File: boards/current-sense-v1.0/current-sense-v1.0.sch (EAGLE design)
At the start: 89 parts, among them IC1 ISO7241, IC2 ISO7241, IC3 ISO7242, IC4 ISO7240, J1 4-PIN_2MM-H, J2 MKS-1658, J3 8-PIN_2MM-H, J6 DF22-2, Q1 IRFH7545, Q2 IRFH7545, Q3 IRFH7545, Q4 IRFH7545, Q5 IRFH7545, Q6 IRFH7545, U1 DRV8303DCA, U13 TLV70233DBVR, U2 INA240PWR, U3 INA240PWR, U4 INA240PWR, U6 ADS8028IRTJT, U7 MPM3620GQV-P, U8 VND5E006ASPTR-E, U9 TLV70450

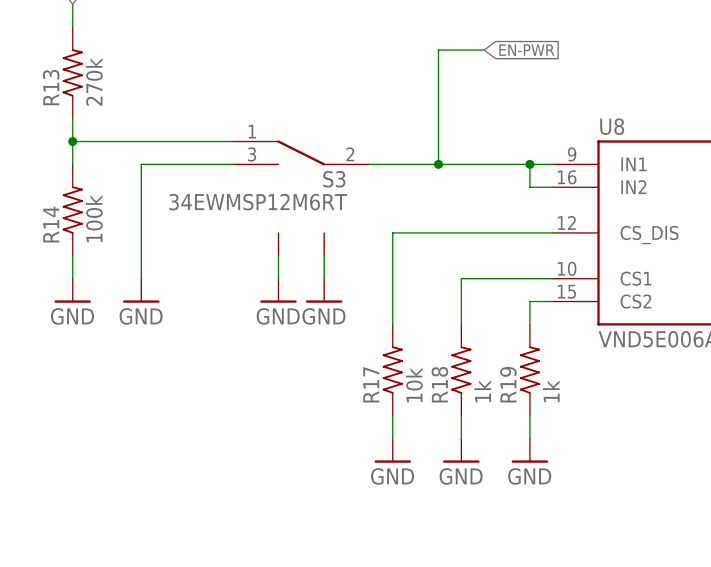
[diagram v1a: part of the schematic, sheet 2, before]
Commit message: removed two ground symbols from board
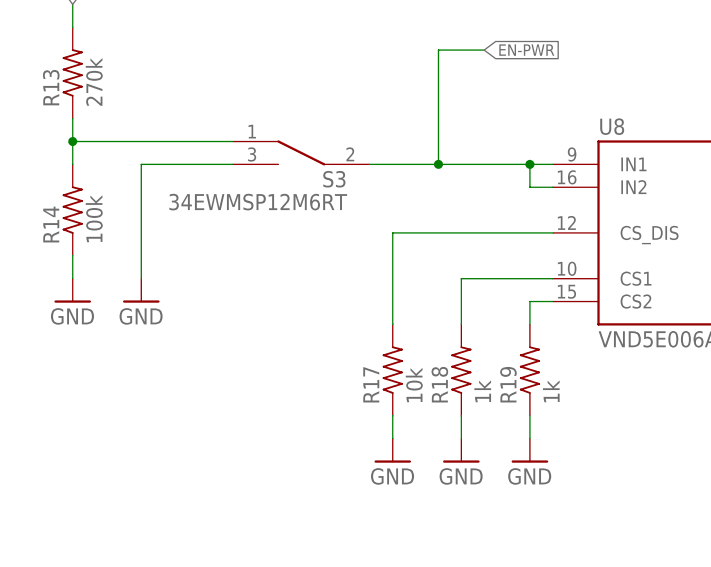
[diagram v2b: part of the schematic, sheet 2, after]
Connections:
- net GND: no longer S3G$2.LEG1, S3G$2.LEG2
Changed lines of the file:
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@@
 <part name="GND65" library="supply1" deviceset="GND" device=""/>
 <part name="S3" library="RoboJackets-Switches" deviceset="34EWMSP12M6RT" device=""/>
-<part name="GND68" library="supply1" deviceset="GND" device=""/>
-<part name="GND69" library="supply1" deviceset="GND" device=""/>
 <part name="GND66" library="supply1" deviceset="GND" device=""/>
 <part name="R22" library="rcl" deviceset="R-US_" device="R0603" value="1k"/>
@@
 <attribute name="VALUE" x="53.34" y="170.18" size="1.778" layer="96" font="vector" rot="MR0"/>
 </instance>
-<instance part="S3" gate="G$2" x="48.26" y="167.64" smashed="yes"/>
-<instance part="GND68" gate="1" x="45.72" y="160.02" smashed="yes">
-<attribute name="VALUE" x="43.18" y="157.48" size="1.778" layer="96"/>
-</instance>
-<instance part="GND69" gate="1" x="50.8" y="160.02" smashed="yes">
-<attribute name="VALUE" x="48.26" y="157.48" size="1.778" layer="96"/>
-</instance>
 <instance part="GND66" gate="1" x="30.48" y="160.02" smashed="yes">
 <attribute name="VALUE" x="27.94" y="157.48" size="1.778" layer="96"/>
@@
 </segment>
 <segment>
-<pinref part="S3" gate="G$2" pin="LEG1"/>
-<pinref part="GND68" gate="1" pin="GND"/>
-<wire x1="45.72" y1="165.1" x2="45.72" y2="162.56" width="0.1524" layer="91"/>
-</segment>
-<segment>
-<pinref part="S3" gate="G$2" pin="LEG2"/>
-<pinref part="GND69" gate="1" pin="GND"/>
-<wire x1="50.8" y1="165.1" x2="50.8" y2="162.56" width="0.1524" layer="91"/>
-</segment>
-<segment>

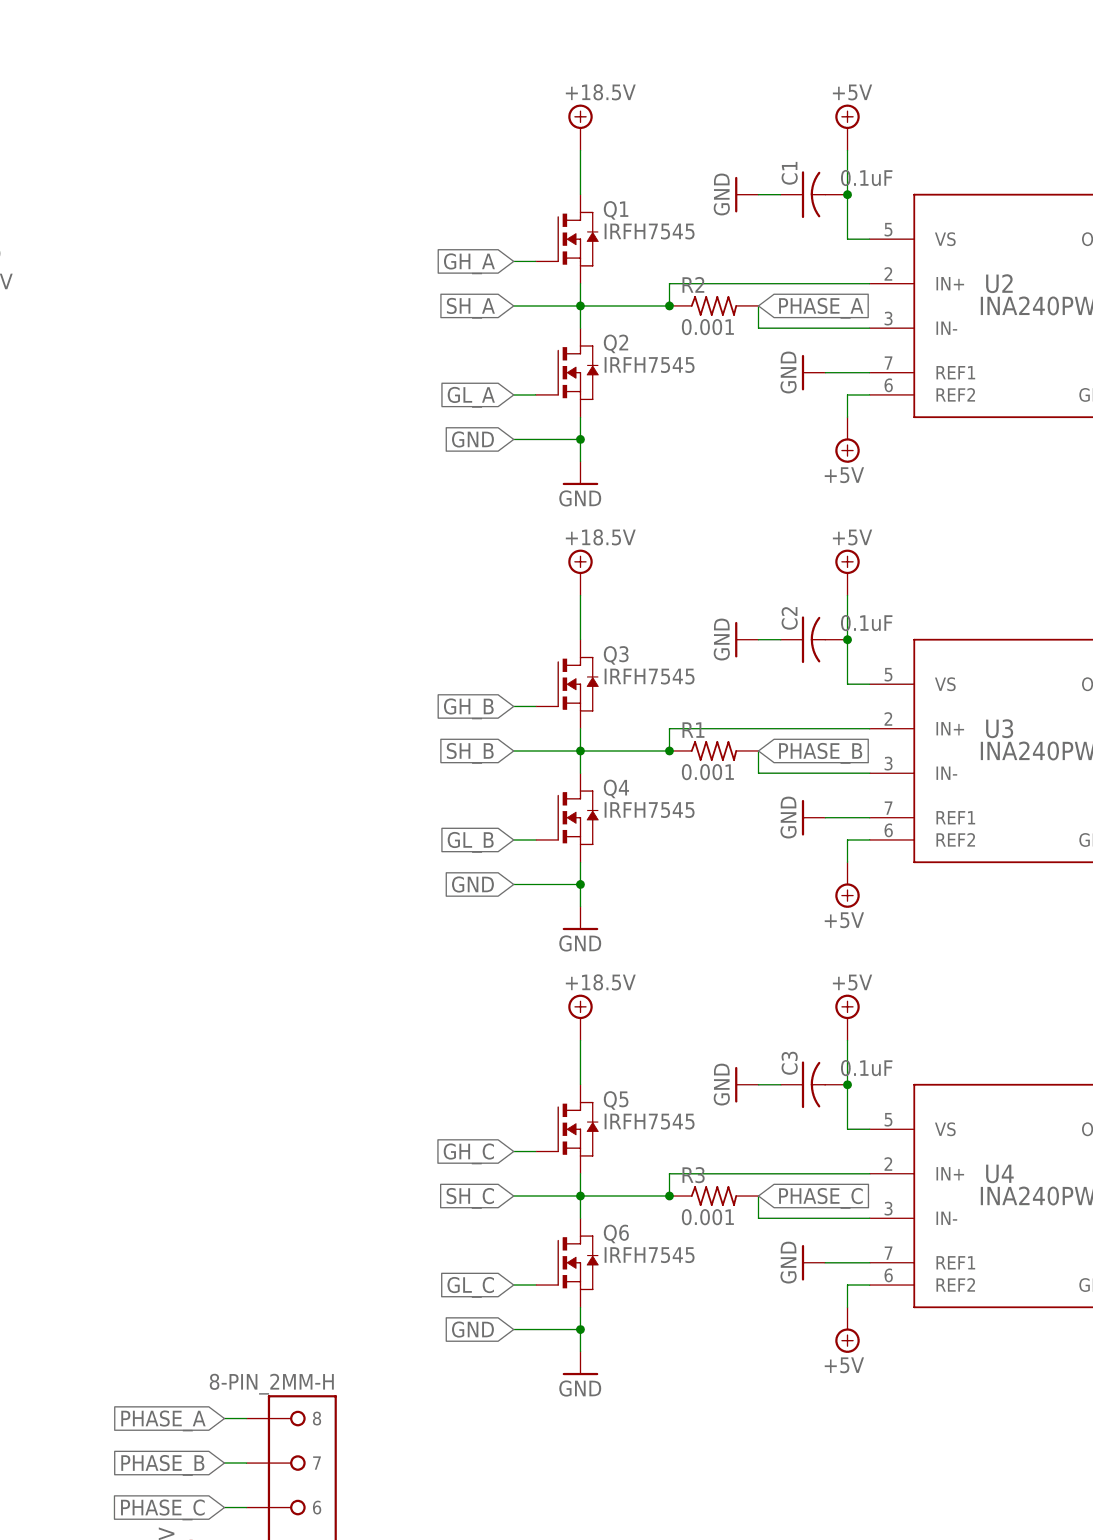
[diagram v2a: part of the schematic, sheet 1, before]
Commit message: changed supply voltage of opamps to 3V3
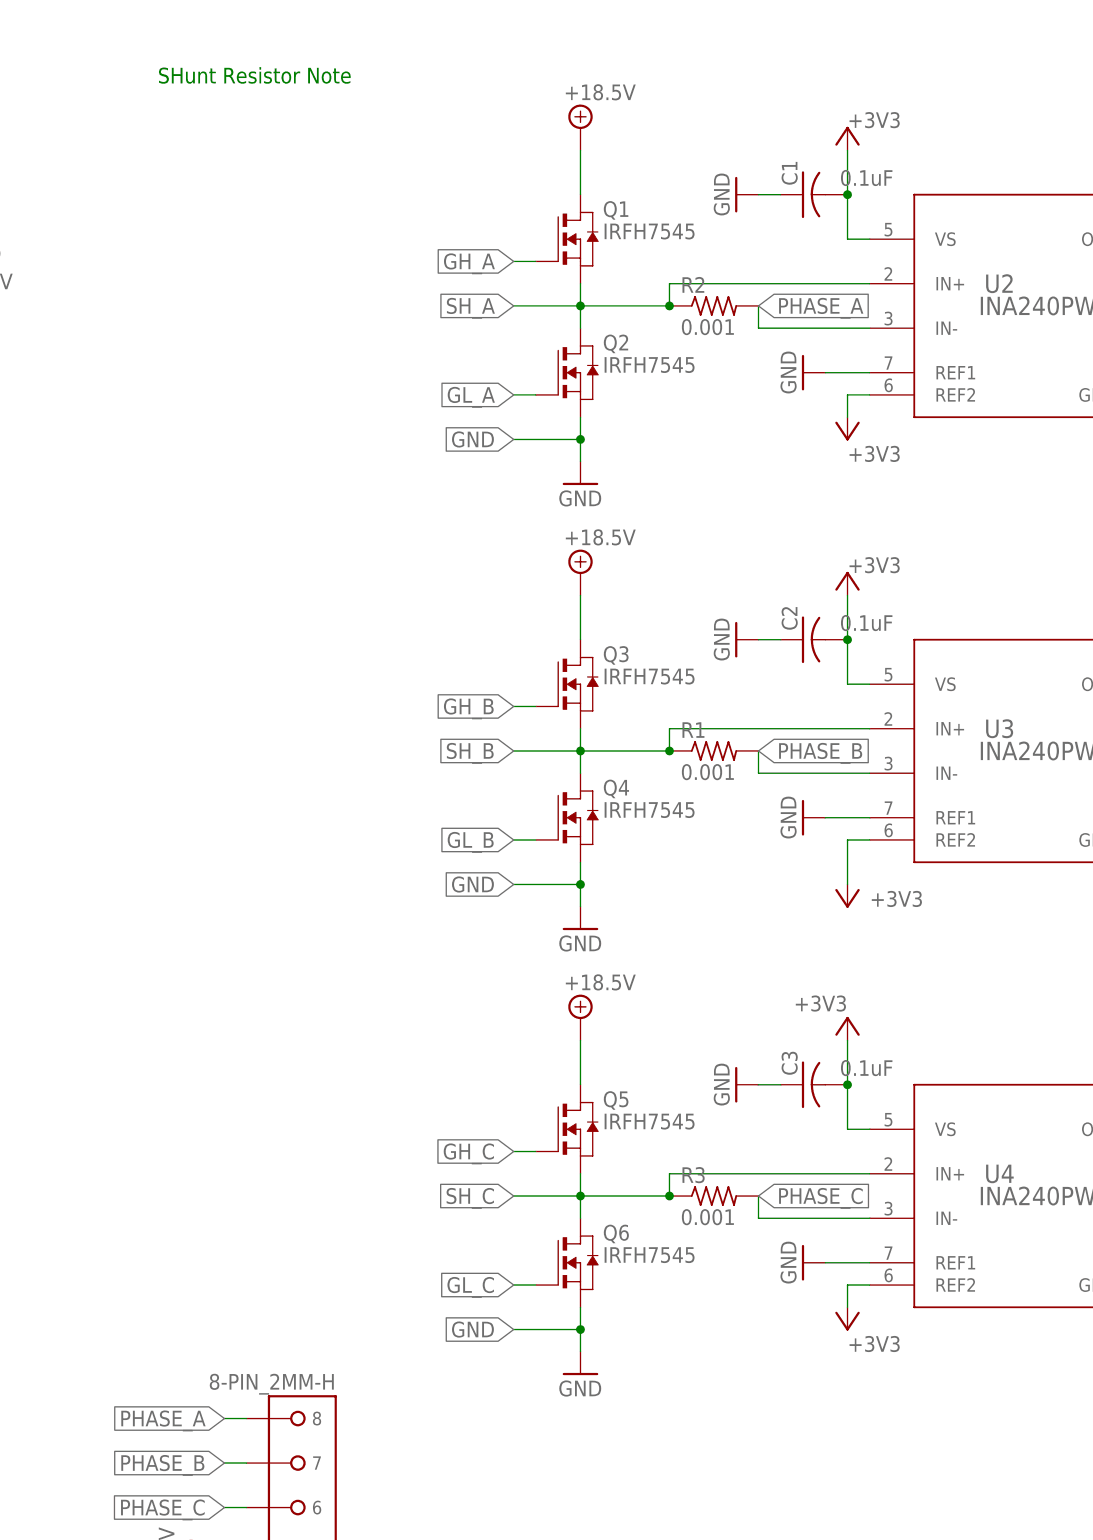
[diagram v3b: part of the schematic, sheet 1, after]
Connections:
- net ADC_5V renamed ADC_3V3
- net +3V3: now also C1.2, C2.2, C3.2, U2.REF2, U2.VS, U3.REF2, U3.VS, U4.REF2, U4.VS
- net +5V: no longer C1.2, C2.2, C3.2, U2.REF2, U2.VS, U3.REF2, U3.VS, U4.REF2, U4.VS
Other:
- note added: "SHunt Resistor Note"

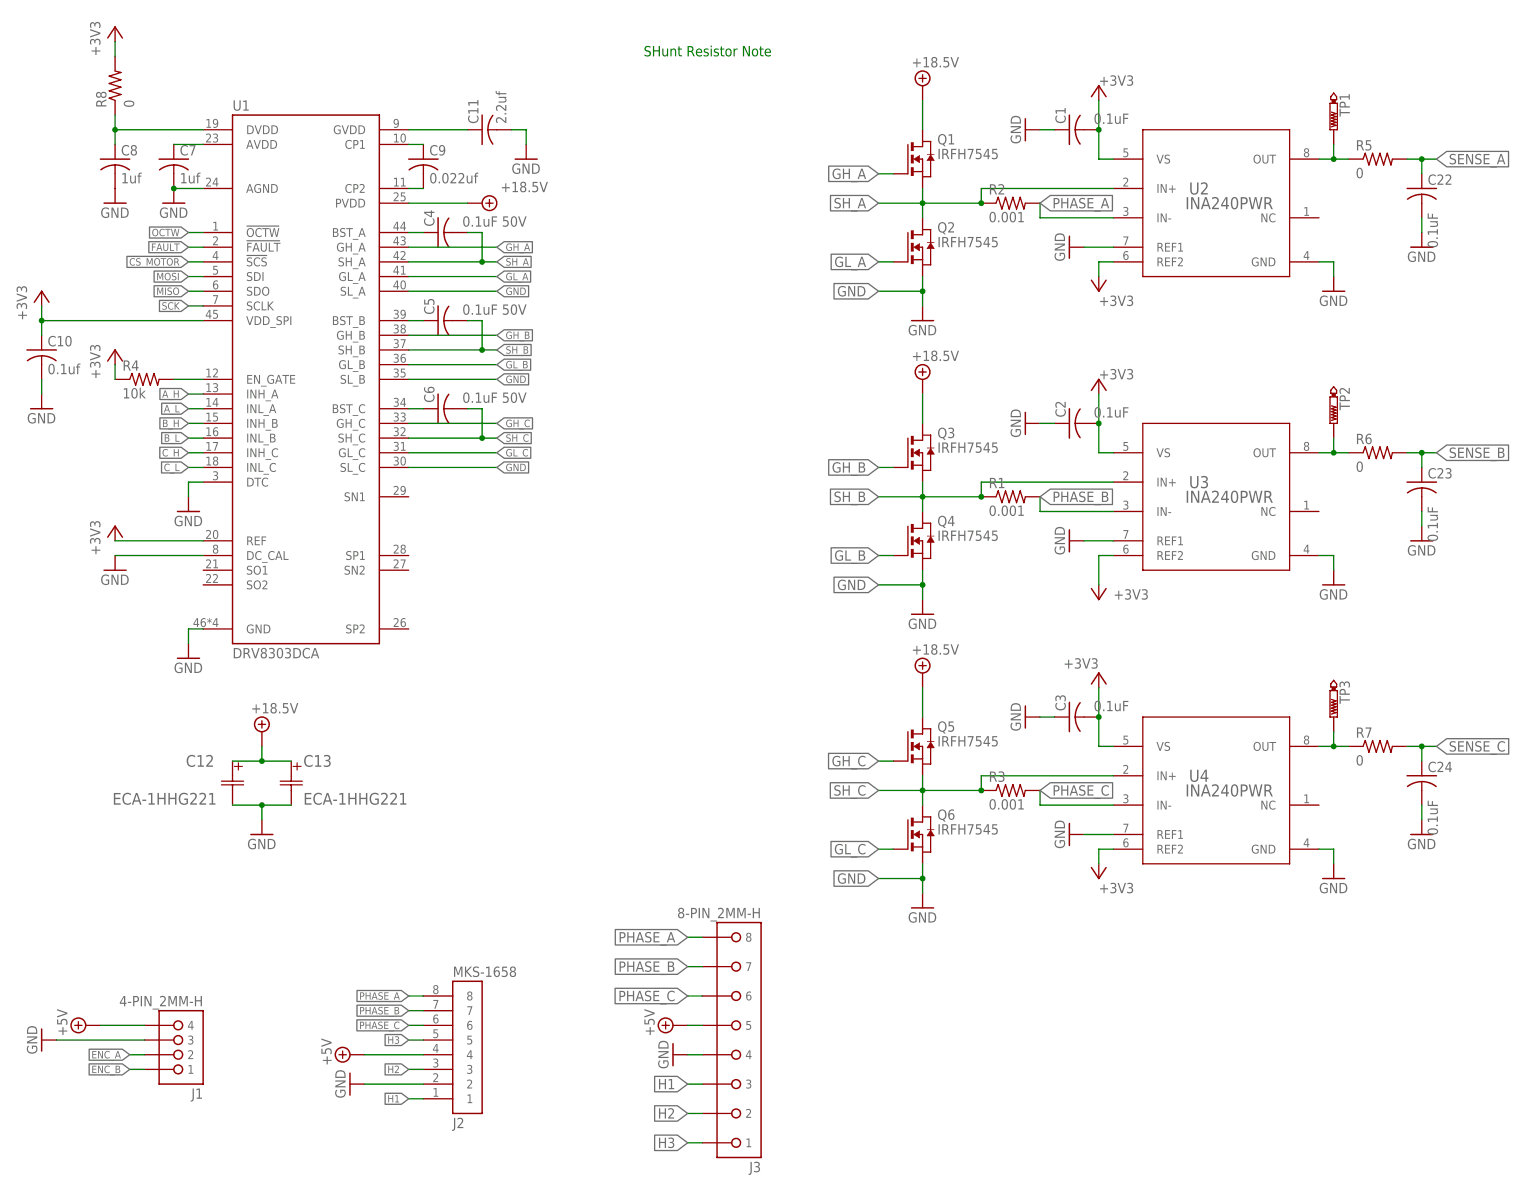
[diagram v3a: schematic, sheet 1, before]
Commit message: added borders in board view
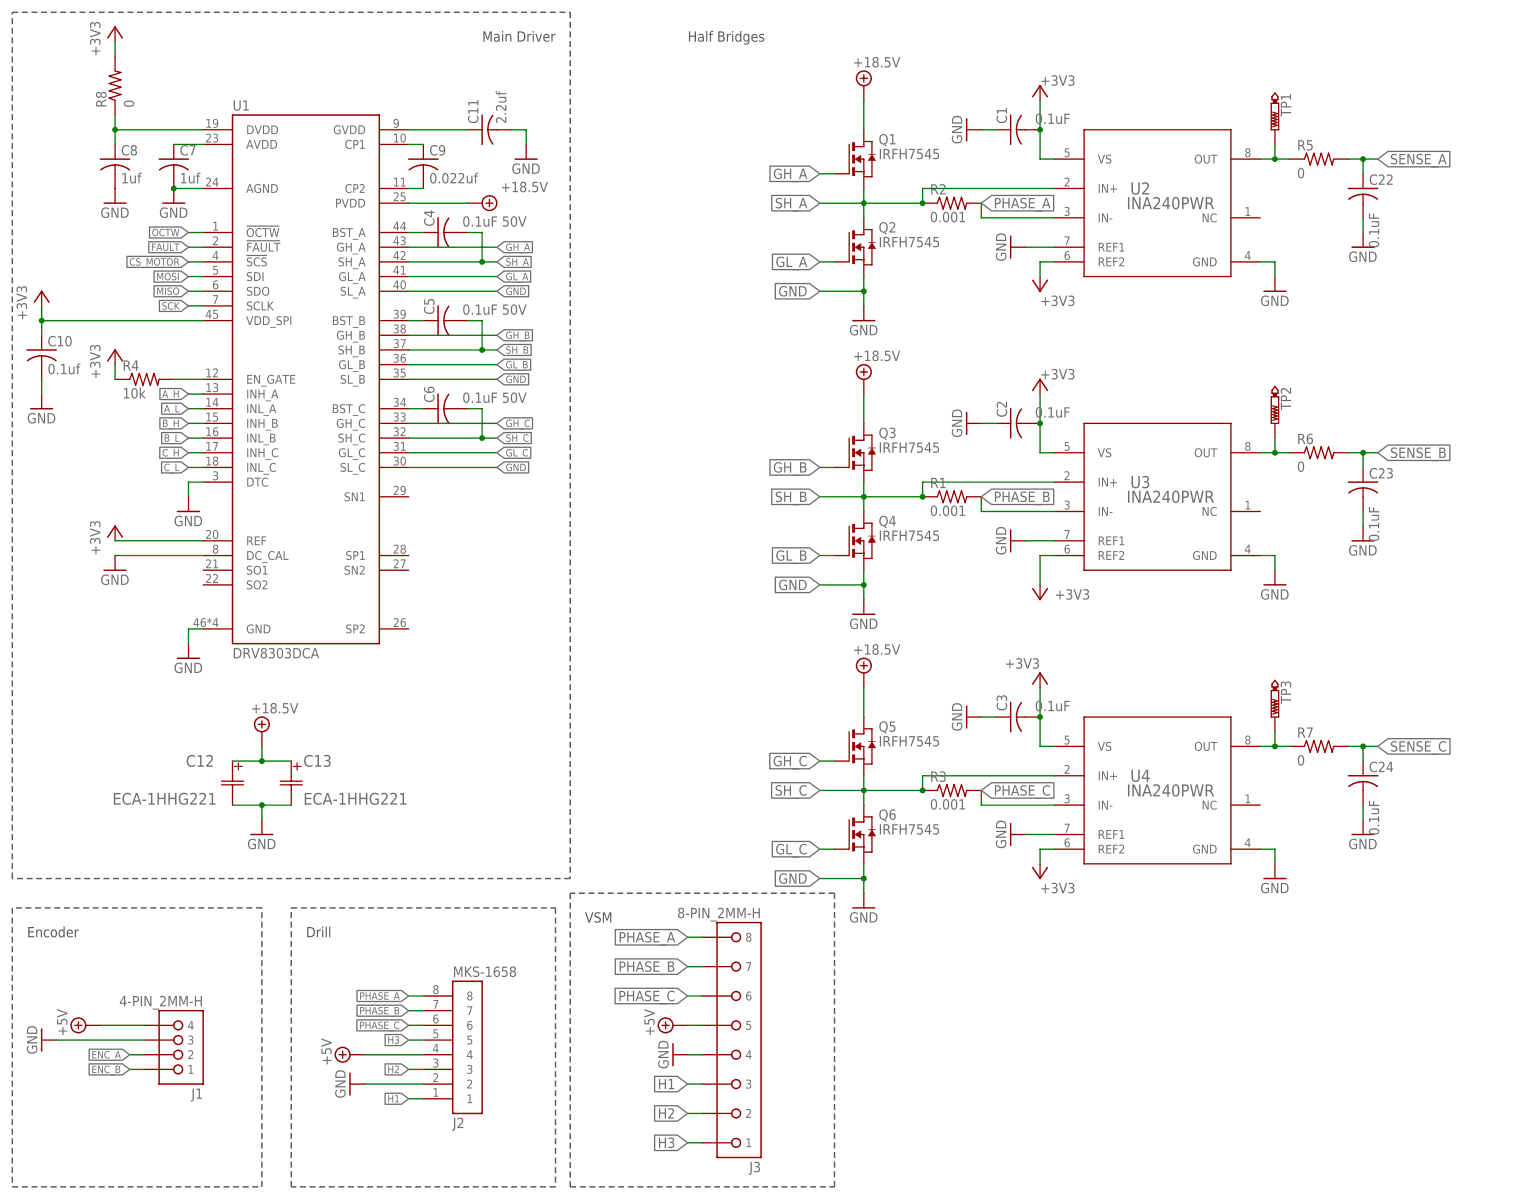
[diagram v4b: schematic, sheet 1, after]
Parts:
- added U5: TLV70233DBVR, RoboJackets-PowerICs:TLV70233DBVR
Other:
- note added: "Drill"
- note added: "Encoder"
- note added: "Half Bridges"
- note added: "Main Driver"
- note added: "VSM"
- note removed: "SHunt Resistor Note"
- moved on the sheet: C1, C2, C22, C23, C24, C3, Q1, Q2, Q3, Q4, Q5, Q6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
